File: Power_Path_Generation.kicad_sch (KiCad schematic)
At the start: 12 parts, among them Q701 PMOS SI2365EDS-T1-GE3, U701 TPS3839G33DQNR, U702 TPS7A0233DQNR

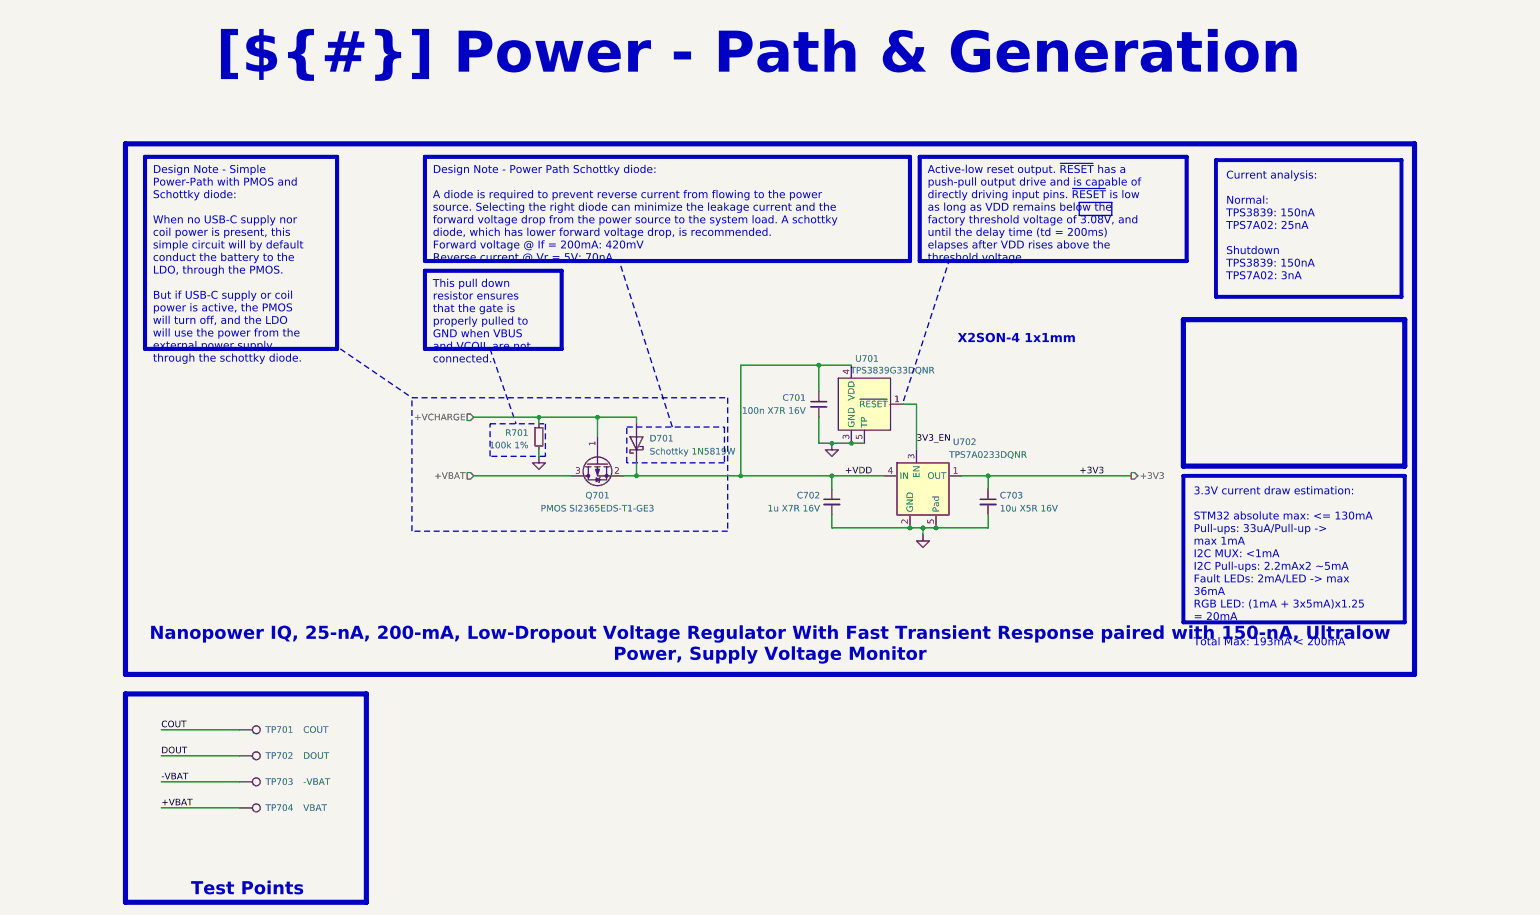
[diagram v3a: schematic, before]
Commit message: Reviewed shematic, cleaned all DRC errors, chosed stackup, started layout
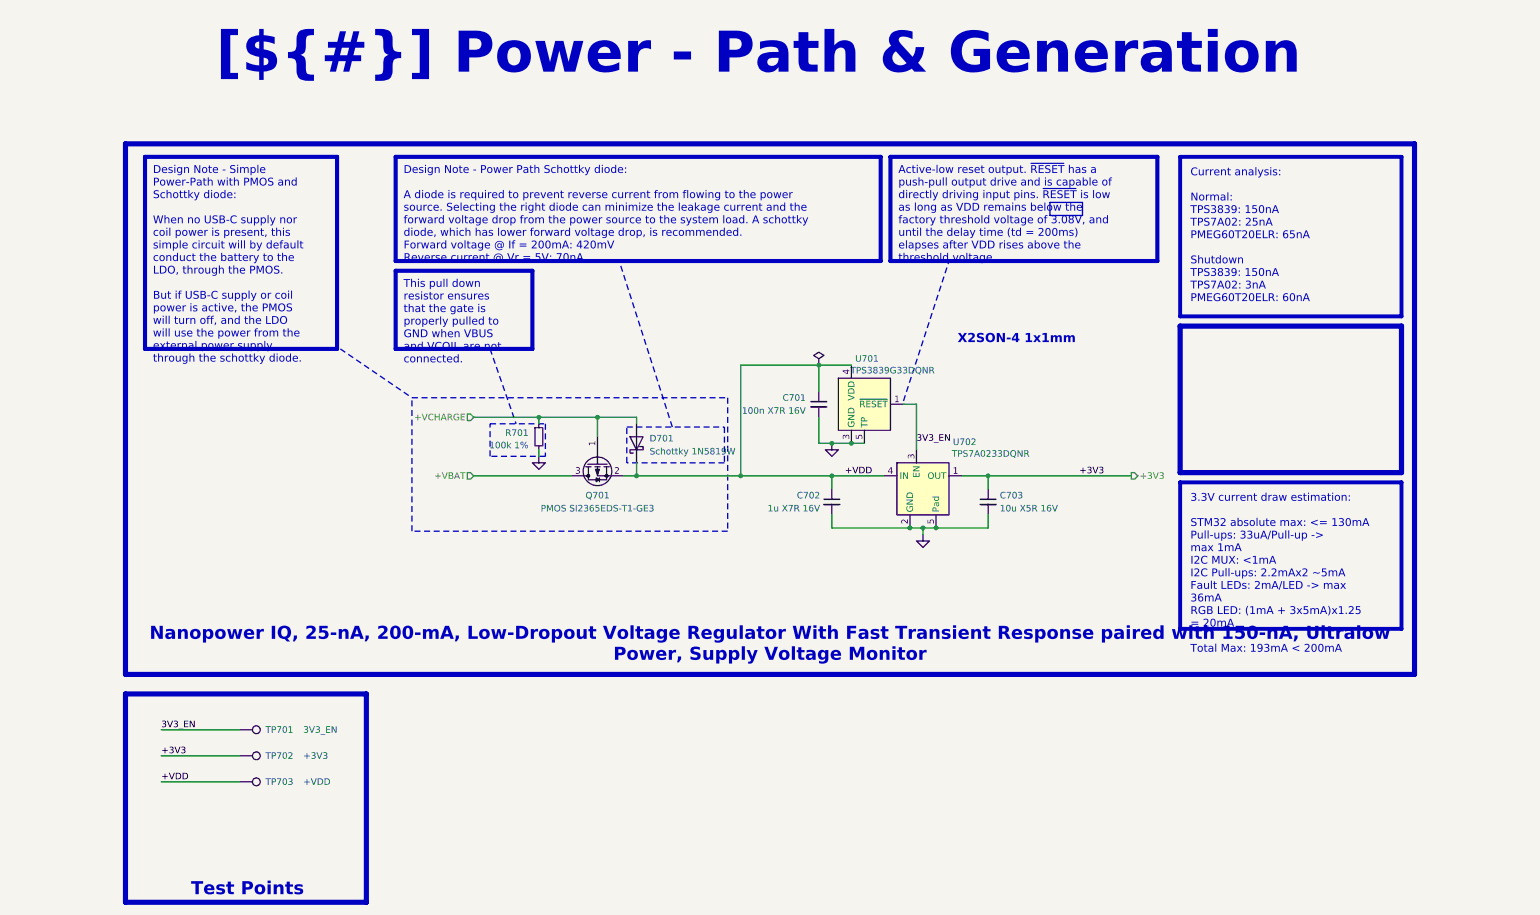
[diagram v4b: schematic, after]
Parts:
- removed TP704: VBAT, 0_Plume:TestPoint_Pad_D0.5mm_Back, symbol Connector:TestPoint
- Q701: symbol Device:Q_PMOS_GSD -> Transistor_FET:Q_PMOS_GSD
- TP701: value COUT -> 3V3_EN
- TP702: value DOUT -> +3V3
- TP703: value -VBAT -> +VDD
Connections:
- net -VBAT is gone; now on net +VDD: TP703.1
- net COUT is gone; now on net 3V3_EN: TP701.1
- net DOUT is gone; now on net +3V3: TP702.1
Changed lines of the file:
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@@
 	)
 	(rectangle
-		(start 210.82 55.88)
-		(end 217.17 58.42)
+		(start 205.105 55.88)
+		(end 211.455 58.42)
 		(stroke
 			(width -0.0001)
@@
 	(text_box "Active-low reset output. ~{RESET} has a push-pull output drive and is capable of directly driving input pins. ~{RESET} is low as long as VDD remains below the factory threshold voltage of 3.08V, and until the delay time (td = 200ms) elapses after VDD rises above the threshold voltage."
 		(exclude_from_sim no)
-		(at 179.705 46.99 0)
+		(at 173.99 46.99 0)
 		(size 52.07 20.32)
 		(margins 1.543 1.543 1.543 1.543)
@@
 	(text_box ""
 		(exclude_from_sim no)
-		(at 231.14 78.74 0)
+		(at 230.505 80.01 0)
 		(size 43.18 28.575)
 		(margins 2.25 2.25 2.25 2.25)
@@
 	(text_box "3.3V current draw estimation:\n\nSTM32 absolute max: <= 130mA\nPull-ups: 33uA/Pull-up -> max 1mA\nI2C MUX: <1mA\nI2C Pull-ups: 2.2mAx2 ~5mA\nFault LEDs: 2mA/LED -> max 36mA\nRGB LED: (1mA + 3x5mA)x1.25 = 20mA\n\nTotal Max: 193mA < 200mA"
 		(exclude_from_sim no)
-		(at 231.14 109.22 0)
+		(at 230.505 110.49 0)
 		(size 43.18 28.575)
 		(margins 2 2 2 2)
@@
 	(text_box "This pull down resistor ensures that the gate is properly pulled to GND when VBUS and VCOIL are not connected."
 		(exclude_from_sim no)
-		(at 83.185 69.215 0)
+		(at 77.47 69.215 0)
 		(size 26.67 15.24)
 		(margins 1.543 1.543 1.543 1.543)
@@
 		)
 	)
-	(text_box "Current analysis:\n\nNormal:\nTPS3839: 150nA\nTPS7A02: 25nA\n\nShutdown\nTPS3839: 150nA\nTPS7A02: 3nA"
+	(text_box "Current analysis:\n\nNormal:\nTPS3839: 150nA\nTPS7A02: 25nA\nPMEG60T20ELR: 65nA\n\nShutdown\nTPS3839: 150nA\nTPS7A02: 3nA\nPMEG60T20ELR: 60nA"
 		(exclude_from_sim no)
-		(at 237.49 47.625 0)
-		(size 36.195 26.67)
+		(at 230.505 46.99 0)
+		(size 43.18 31.115)
 		(margins 2 2 2 2)
 		(stroke
@@
 	(text_box "Design Note - Power Path Schottky diode:\n\nA diode is required to prevent reverse current from flowing to the power source. Selecting the right diode can minimize the leakage current and the forward voltage drop from the power source to the system load. A schottky diode, which has lower forward voltage drop, is recommended.\nForward voltage @ If = 200mA: 420mV\nReverse current @ Vr = 5V: 70nA"
 		(exclude_from_sim no)
-		(at 83.185 46.99 0)
+		(at 77.47 46.99 0)
 		(size 94.615 20.32)
 		(margins 1.543 1.543 1.543 1.543)
@@
 		)
 	)
-	(wire
-		(pts
-			(xy 31.75 173.99) (xy 46.99 173.99)
-		)
-		(stroke
-			(width 0)
-			(type default)
-		)
-	)
 	(polyline
 		(pts
@@
 	)
 	(image
-		(at 252.73 92.71)
+		(at 252.095 93.98)
 		(scale 0.181984)
 		(data "iVBORw0KGgoAAAANSUhEUgAABP4AAANCCAYAAAD2rwJAAAAMTmlDQ1BJQ0MgUHJvZmlsZQAASImV"
@@
 			"L1B6OC9QejgvUHo4L1B6OC9QejgvUHo4L1B6OC9QejgvUHo4L1B6OC9QejgvUHo4L1B6OC9Qejgv"
 			"UHo4L1B6OC9QejgvUHo4L1B6OC9QejgvUHo4L1B6OC9QejgvUHo4L1B6OC9QejgvUHo4L1B6OC9Q"
-			"ejgvUHo4L1B6OC9QejgvUHo4L1B6OC9QejgvUHo4L1B6OC9OaHB0TWFnYw=="
+			"ejgvUHo4L1B6OC9QejgvUHo4L1B6OC9QejgvUHo4L1B6OC9OaHB0TWFnYwAAUQAAAEYAAABxAAAA"
+			"awAAADQAAABaAAAAUwAAAEUAAAA5AAAAUgAAAEEAAABGAAAAQQAAADYAAABWAAAAVAAAADcAAAAx"
+			"AAAAZAAAACsAAAArAAAAKwAAAFUAAAAxAAAAaQAAAGwAAAA3AAAAQQAAAG0AAABYAAAAdAAAAEUA"
+			"AABXAAAASgAAAEcAAABUAAAAawAAAGoAAABRAAAAQgAAAFcAAAB3AAAAKwAAAEoAAABVAAAAeQAA"
+			"AHcAAABQAAAANQAAAHYAAABWAAAAOQAAACsAAAByAAAARAAAAEcAAABUAAAAcQAAAHoAAABHAAAA"
+			"TgAAADcAAABXAAAAYQAAAGUAAABrAAAAQQAAAEgAAABhAAAATgAAAGcAAABCAAAAVwAAADMAAABm"
+			"AAAANgAAAG8AAAA4AAAAUQAAAHQAAABOAAAAQwAAAEwAAABRAAAAKwAAAHgAAAByAAAAOAAAAFEA"
+			"AABzAAAAYgAAADUAAAByAAAAUQAAAEIAAAAzAAAAUgAAAGkAAABPAAAAZAAAAEMAAABjAAAAdAAA"
+			"AFQAAABqAAAARQAAAGMAAABsAAAAZAAAAG4AAABIAAAAbAAAAFEAAAA5AAAAcAAAAEEAAAAwAAAA"
+			"dgAAADYAAAAyAAAAbwAAACsAAAA3AAAAdQAAAEIAAAB3AAAAeQAAADIAAABBAAAATwAAAFAAAAA2"
+			"AAAASQAAAE4AAABGAAAAdAAAAGUAAABXAAAAbQAAAEIAAABaAAAAagAAAG0AAAA1AAAAbAAAADUA"
+			"AAAwAAAAdwAAAGQAAAA3AAAARwAAAHEAAABDAAAAbQAAAEwAAABZAAAAQwAAAEYAAABNAAAAbAAA"
+			"AHAAAAA0AAAASgAAADUAAAAvAAAAawAAAFYAAAB6AAAAegAAAFAAAABNAAAAbQAAADIAAAB2AAAA"
+			"VwAAAEEAAABaAAAAVQAAAGUAAABtAAAAZwAAADMAAABlAAAAVgAAAGIAAAB3AAAASwAAAGkAAABy"
+			"AAAAbAAAAEsAAAAvAAAAVAAAAFgAAABXAAAAUAAAAFgAAABzAAAAdAAAAC8AAABiAAAAegAAADQA"
+			"AABlAAAANAAAADgAAAB1AAAAMgAAADMAAABNAAAAMgAAACsAAABmAAAAbQAAAGUAAABiAAAAcgAA"
+			"AGoAAABzAAAATAAAAEYAAAAvAAAAUAAAAHgAAABjAAAAOAAAADUAAAAvAAAASAAAAEcAAAA4AAAA"
+			"UQAAADMAAAB6AAAANgAAAG4AAAB6AAAANgAAAE8AAABaAAAANQAAAHoAAABQAAAAOAAAAGIAAABw"
+			"AAAAMgAAADYAAABDAAAASAAAADUAAABUAAAATgAAAGYAAABiAAAAcgAAAA=="
 		)
 	)
@@
 			"8AAAAAAAAAACAAAAAwAAAAEAAAAEAAAABQAAAAQAAAAAAAAABAAAAAAAAAAEAAAAAAAAAAQAAAAA"
 			"AAAABAAAAAAAAAAEAAAAAAAAAMCAAAACAAAAAAAAACAAAAAgAAAAHQAAAAEAAAAAAAAAoAAAAAUA"
-			"AAA8AAAAYA=="
+			"AAA8AAAAYG4AAABzAAAASgAAAGIAAABDAAAAWAAAAHcAAABGAAAANAAAAEMAAABQAAAANgAAAHcA"
+			"AABFAAAAeAAAAG0AAAB2AAAANgAAAE0AAAAyAAAAbAAAAG8AAABBAAAAbwAAAHUAAABEAAAAbwAA"
+			"AG4AAAA0AAAAZAAAAGcAAABwAAAAegAAAGwAAABOAAAAMgAAAGYAAABrAAAAWAAAAHcAAAA5AAAA"
+			"OAAAAC8AAAB6AAAAWQAAAEUAAABuAAAAdgAAAEkAAABhAAAAKwAAAE8AAABzAAAAUQAAAGMAAAB5"
+			"AAAANgAAADIAAABRAAAARQAAAE8AAABDAAAAWQAAAFQAAABuAAAAZAAAAG4AAABCAAAAYgAAADQA"
+			"AABKAAAANAAAAG0AAABXAAAAZwAAAGQAAAB1AAAANQAAAEEAAABYAAAAeAAAAHoAAABDAAAAaAAA"
+			"AEMAAABSAAAAOAAAAEMAAABxAAAASgAAAGoAAAAzAAAASAAAAE0AAABoAAAAaQAAAFEAAABEAAAA"
+			"ZAAAAEIAAAB3AAAAMAAAAEQAAABrAAAAVAAAAGcAAAAyAAAANAAAAHkAAAAvAAAAZwAAADMAAAB4"
+			"AAAAZwAAAHUAAABlAAAAOQAAAGoAAABKAAAAbwAAAHMAAAB5AAAAQQAAAHEAAABkAAAAYwAAAG4A"
+			"AAB1AAAAdAAAAE8AAABjAAAAbgAAAEEAAABpAAAAMQAAAE8AAAAwAAAAcwAAAHAAAABUAAAAaAAA"
+			"AFMAAABZAAAAUAAAAGoAAABOAAAAYQAAAGIAAABKAAAAQgAAAFAAAAA2AAAAZQAAAGIAAABnAAAA"
+			"eQAAAHgAAABRAAAAUAAAAFkAAAAyAAAARAAAAFkAAABVAAAAKwAAAHUAAABtAAAAOQAAADEAAAB3"
+			"AAAAUAAAADcAAABNAAAAVQAAAHMAAABsAAAAeQAAAFMAAAAwAAAAOAAAAFoAAABaAAAANgAAAHUA"
+			"AAB5AAAATAAAAEIAAABIAAAAVgAAAG0AAABzAAAAUgAAAEgAAABlAAAATwAAAE4AAABLAAAAVAAA"
+			"AGMAAABQAAAAZwAAADYAAABTAAAALwAAAHIAAAArAAAANQAAAFoAAAA5AAAAKwAAAHYAAABmAAAA"
+			"dgAAADEAAAByAAAAMwAAACsAAAA5AAAAZQAAAHoAAABPAAAASgAAAE0AAABrAAAAcwAAAFgAAABC"
+			"AAAAWAAAAGYAAAA4AAAAQwAAAEkAAABFAAAAawAAAG8AAABpAAAAYgAAAFoAAABNAAAAUQAAADcA"
+			"AABwAAAAMAAAAFoAAABIAAAAcAAAADgAAAArAAAAUAAAAFEAAABOAAAAaQAAAG0AAABWAAAASQAA"
+			"AEkAAABZAA=="
 		)
 	)
@@
 		)
 	)
-	(label "DOUT"
+	(label "+3V3"
 		(at 31.75 163.83 0)
 		(effects
@@
 		)
 	)
-	(label "COUT"
+	(label "3V3_EN"
 		(at 31.75 158.75 0)
 		(effects
@@
 		)
 	)
-	(label "-VBAT"
+	(label "+VDD"
 		(at 31.75 168.91 0)
 		(effects
@@
 		)
 	)
-	(label "+VBAT"
-		(at 31.75 173.99 0)
-		(effects
-			(font
-				(size 1.27 1.27)
-				(color 132 0 0 1)
-			)
-			(justify left bottom)
-		)
-	)
 	(label "3V3_EN"
 		(at 179.07 102.87 0)
@@
 	)
 	(symbol
-		(lib_id "Device:Q_PMOS_GSD")
+		(lib_id "power:PWR_FLAG")
+		(at 160.02 87.63 0)
+		(unit 1)
+		(exclude_from_sim no)
+		(in_bom yes)
+		(on_board yes)
+		(dnp no)
+		(fields_autoplaced yes)
+		(property "Reference" "#FLG0701"
+			(at 160.02 85.725 0)
+			(effects
+				(font
+					(size 1.27 1.27)
+				)
+				(hide yes)
+			)
+		)
+		(property "Value" "PWR_FLAG"
+			(at 160.02 82.55 0)
+			(effects
+				(font
+					(size 1.27 1.27)
+				)
+				(hide yes)
+			)
+		)
+		(property "Footprint" ""
+			(at 160.02 87.63 0)
+			(effects
+				(font
+					(size 1.27 1.27)
+				)
+				(hide yes)
+			)
+		)
+		(property "Datasheet" "~"
+			(at 160.02 87.63 0)
+			(effects
+				(font
+					(size 1.27 1.27)
+				)
+				(hide yes)
+			)
+		)
+		(property "Description" "Special symbol for telling ERC where power comes from"
+			(at 160.02 87.63 0)
+			(effects
+				(font
+					(size 1.27 1.27)
+				)
+				(hide yes)
+			)
+		)
+		(pin "1"
+		)
+		(instances
+			(project "Plume"
+				(path "/0650c7a8-acba-429c-9f8e-eec0baf0bc1c/fede4c36-00cc-4d3d-b71c-5243ba232202/1d8841d3-b2be-4035-b859-53b06135dc6a"
+					(reference "#FLG0701")
+					(unit 1)
+				)
+			)
+		)
+	)
+	(symbol
+		(lib_id "Transistor_FET:Q_PMOS_GSD")
 		(at 116.84 106.68 90)
 		(mirror x)
@@
 		)
 		(property "Value" "TPS7A0233DQNR"
-			(at 193.04 105.1111 0)
+			(at 193.548 104.902 0)
 			(effects
 				(font
@@
 			)
 		)
-		(property "Value" "-VBAT"
+		(property "Value" "+VDD"
 			(at 59.436 168.91 90)
 			(effects
@@
 	(symbol
 		(lib_id "Connector:TestPoint")
-		(at 46.99 173.99 270)
-		(mirror x)
-		(unit 1)
-		(exclude_from_sim no)
-		(in_bom no)
-		(on_board yes)
-		(dnp no)
-		(property "Reference" "TP704"
-			(at 52.07 173.99 90)
-			(effects
-				(font
-					(size 1.27 1.27)
-				)
-				(justify left)
-			)
-		)
-		(property "Value" "VBAT"
-			(at 59.436 173.99 90)
-			(effects
-				(font
-					(size 1.27 1.27)
-				)
-				(justify left)
-			)
-		)
-		(property "Footprint" "0_Plume:TestPoint_Pad_D0.5mm_Back"
-			(at 46.99 168.91 0)
-			(effects
-				(font
-					(size 1.27 1.27)
-				)
-				(hide yes)
-			)
-		)
-		(property "Datasheet" "~"
-			(at 46.99 168.91 0)
-			(effects
-				(font
-					(size 1.27 1.27)
-				)
-				(hide yes)
-			)
-		)
-		(property "Description" "test point"
-			(at 46.99 173.99 0)
-			(effects
-				(font
-					(size 1.27 1.27)
-				)
-				(hide yes)
-			)
-		)
-		(property "Manufacturer Part Number" ""
-			(at 46.99 173.99 0)
-			(effects
-				(font
-					(size 1.27 1.27)
-				)
-				(hide yes)
-			)
-		)
-		(property "Supplier" ""
-			(at 46.99 173.99 0)
-			(effects
-				(font
-					(size 1.27 1.27)
-				)
-				(hide yes)
-			)
-		)
-		(pin "1"
-		)
-		(instances
-			(project "Plume"
-				(path "/0650c7a8-acba-429c-9f8e-eec0baf0bc1c/fede4c36-00cc-4d3d-b71c-5243ba232202/1d8841d3-b2be-4035-b859-53b06135dc6a"
-					(reference "TP704")
-					(unit 1)
-				)
-			)
-		)
-	)
-	(symbol
-		(lib_id "Connector:TestPoint")
 		(at 46.99 163.83 270)
 		(mirror x)
@@
 			)
 		)
-		(property "Value" "DOUT"
+		(property "Value" "+3V3"
 			(at 59.436 163.83 90)
 			(effects
@@
 			)
 		)
-		(property "Value" "COUT"
+		(property "Value" "3V3_EN"
 			(at 59.436 158.75 90)
 			(effects

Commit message: Advanced rough layout
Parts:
- removed C702: 1u X7R 16V, Capacitor_SMD:C_0603_1608Metric, symbol Device:C_Small
- added C704: 10u X5R 16V, Capacitor_SMD:C_0603_1608Metric, symbol Device:C_Small
- U702: value TPS7A0233DQNR -> TPS7A0233DBVR; footprint Package_SON:Texas_X2SON-4_1x1mm_P0.65mm -> Package_TO_SOT_SMD:SOT-23-5; symbol 0_Plume:TPS7A20xxxDQN -> 0_Plume:TPS7A20xxxDBVR; Manufacturer Part Number TPS7A0233DQNR -> TPS7A0233DBVR; Supplier Part Number 595-TPS7A0233DQNR -> 595-TPS7A0233DBVR
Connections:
- net +VDD: now also C704.1
- net GND: now also C704.2
